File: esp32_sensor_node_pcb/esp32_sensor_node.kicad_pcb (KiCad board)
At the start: 2 copper layers, 50 x 60 mm, 27 parts, among them J1 Conn_02x10_Top_Bottom, Q1 2N7002K, SW1 SW_DIP_x01, SW2 SW_DIP_x01, U1 HT7833, U2 ESP32-WROOM-E, U3 MAX3483AEASA+

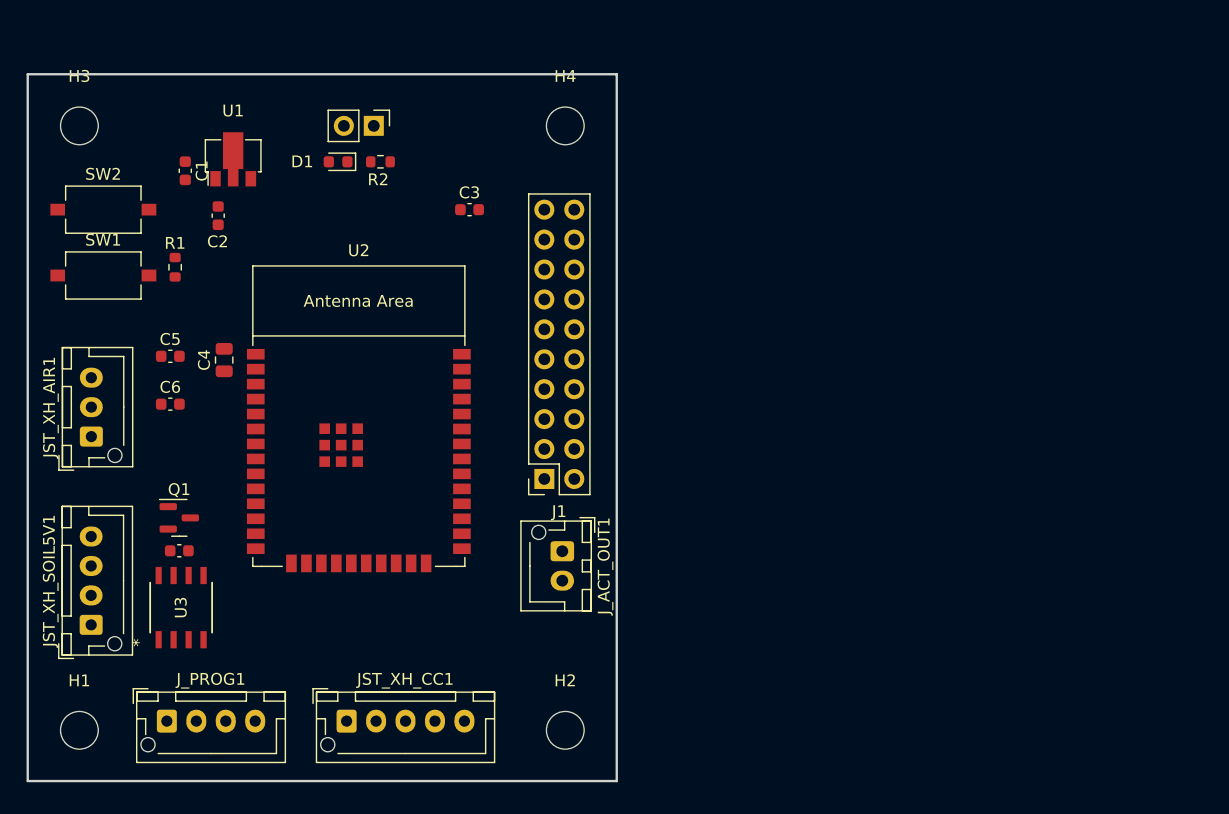
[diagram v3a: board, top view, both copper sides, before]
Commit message: Complete first draft routing
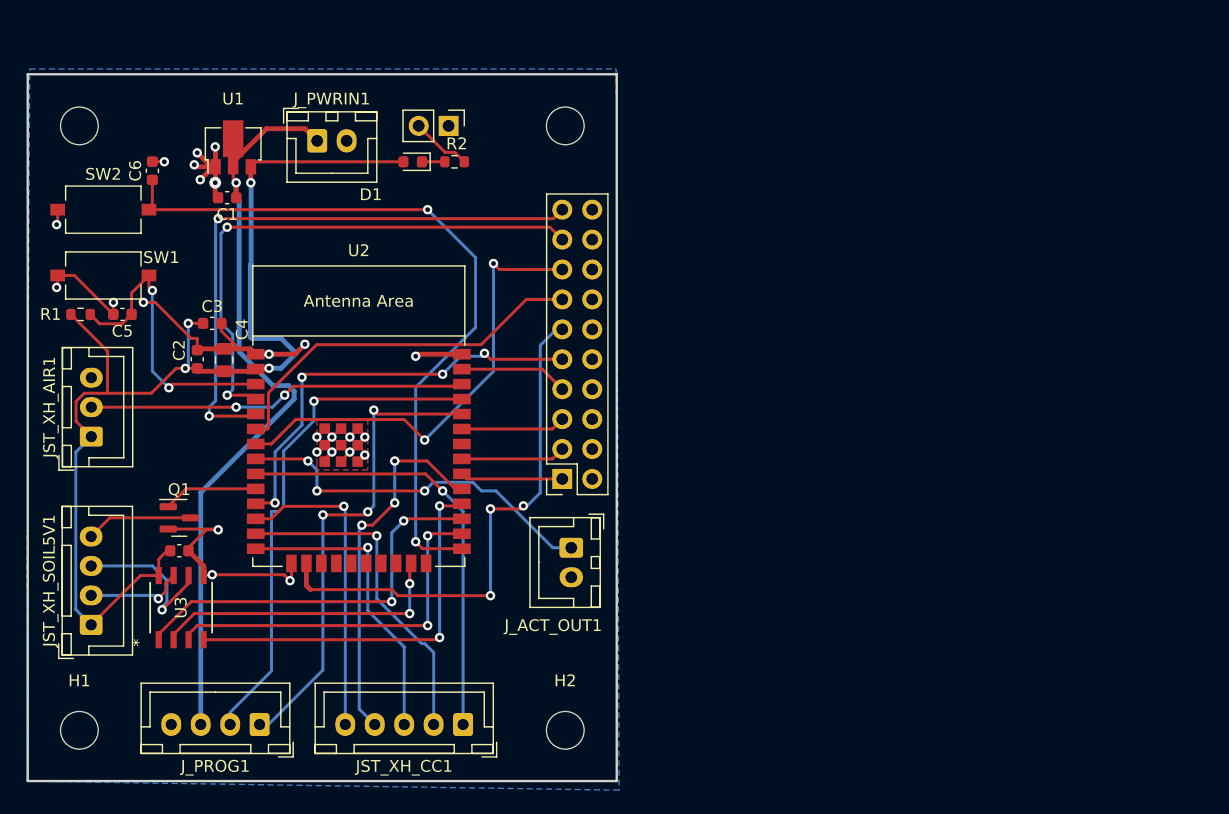
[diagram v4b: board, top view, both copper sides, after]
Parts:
- added J_PWRIN1: Conn_01x02_Socket, Connector_JST:JST_XH_B2B-XH-A_1x02_P2.50mm_Vertical, F.Cu at (44.6, 25.7)
- J1: value Conn_02x10_Top_Bottom -> Conn_02x10_Odd_Even
- JST_XH_AIR1: footprint Connector_JST:JST_XH_B3B-XH-AM_1x03_P2.50mm_Vertical -> Connector_JST:JST_XH_B3B-XH-A_1x03_P2.50mm_Vertical
- JST_XH_CC1: footprint Connector_JST:JST_XH_B5B-XH-AM_1x05_P2.50mm_Vertical -> Connector_JST:JST_XH_B5B-XH-A_1x05_P2.50mm_Vertical
- JST_XH_SOIL5V1, J_PROG1: footprint Connector_JST:JST_XH_B4B-XH-AM_1x04_P2.50mm_Vertical -> Connector_JST:JST_XH_B4B-XH-A_1x04_P2.50mm_Vertical
- J_ACT_OUT1: footprint Connector_JST:JST_XH_B2B-XH-AM_1x02_P2.50mm_Vertical -> Connector_JST:JST_XH_B2B-XH-A_1x02_P2.50mm_Vertical
- moved C3 23.9 mm to (35.7, 41.1)
- moved C6 19.9 mm to (30.6, 28.2), turned to 90 degrees
- moved C2 12.3 mm to (34.4, 44.2), turned to 90 degrees
- moved JST_XH_CC1 9.89 mm to (57.0, 75.2), turned to 180 degrees
- moved R1 8.97 mm to (24.5, 40.4), turned to 0 degrees
- moved J_PROG1 7.88 mm to (39.7, 75.2), turned to 180 degrees
- moved JP1 6.35 mm to (55.7, 24.4)
- moved D1 6.33 mm to (52.7, 27.4)
- moved R2 6.29 mm to (56.2, 27.4), turned to 180 degrees
- moved C5 5.40 mm to (28.0, 40.4), turned to 180 degrees
- moved C1 4.23 mm to (36.9, 30.5), turned to 180 degrees
- moved J1 1.52 mm to (65.4, 54.4)
- moved U1 1.02 mm to (37.4, 25.9)
- moved J_ACT_OUT1 0.82 mm to (66.1, 60.2)
- turned C7_MAXDECOUP1 to 0 degrees
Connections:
- J1 pad 10: GPIO39 -> GND
- J1 pad 11: GND -> GPIO13
- J1 pad 13: GND -> GPIO34
- J1 pad 15: GND -> GPIO35
- J1 pad 17: GND -> GPIO36
- J1 pad 19: GND -> GPIO39
- J1 pad 2: GPIO19 -> GND
- J1 pad 3: GPIO21 -> GPIO19
- J1 pad 4: GPIO23 -> GND
- J1 pad 5: GPIO26 -> GPIO21
- J1 pad 6: GPIO13 -> GND
- J1 pad 7: GPIO34 -> GPIO23
- J1 pad 8: GPIO35 -> GND
- J1 pad 9: GPIO36 -> GPIO26
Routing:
- net +3.3V: track 0.00 -> 96.2 mm, vias 0 -> 4
- net GND: track 0.00 -> 69.6 mm, vias 0 -> 24
- net +5V: track 0.00 -> 64.7 mm, vias 0 -> 1
- net GPIO0/BOOT: track 0.00 -> 62.0 mm, vias 0 -> 2
- net GPIO39: track 0.00 -> 50.4 mm, vias 0 -> 2
- net GPIO36: track 0.00 -> 46.5 mm, vias 0 -> 2
- net GPIO13: track 0.00 -> 44.5 mm, vias 0 -> 3
- net Net-(J_PROG1-Pin_2): track 0.00 -> 44.1 mm, vias 0 -> 1
- net Net-(J_PROG1-Pin_1): track 0.00 -> 41.1 mm, vias 0 -> 3
- net GPIO35: track 0.00 -> 39.4 mm, vias 0 -> 2
- net ACT_IN: track 0.00 -> 37.0 mm, vias 0 -> 1
- net GPIO26: track 0.00 -> 36.3 mm, vias 0 -> 4
- net Net-(U2-GPIO16): track 0.00 -> 33.2 mm, vias 0 -> 2
- net Net-(U2-GPIO17): track 0.00 -> 33.0 mm, vias 0 -> 2
- net GPIO34: track 0.00 -> 32.3 mm
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- added copper zone on B.Cu, net GND
- added copper zone on F.Cu, net GND

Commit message: Changed schematic - 3.3V to RS485, 5V to Soil sensor. Changed resistor from 1.9k to 4.7k. Finished routing of PCB with new schematic
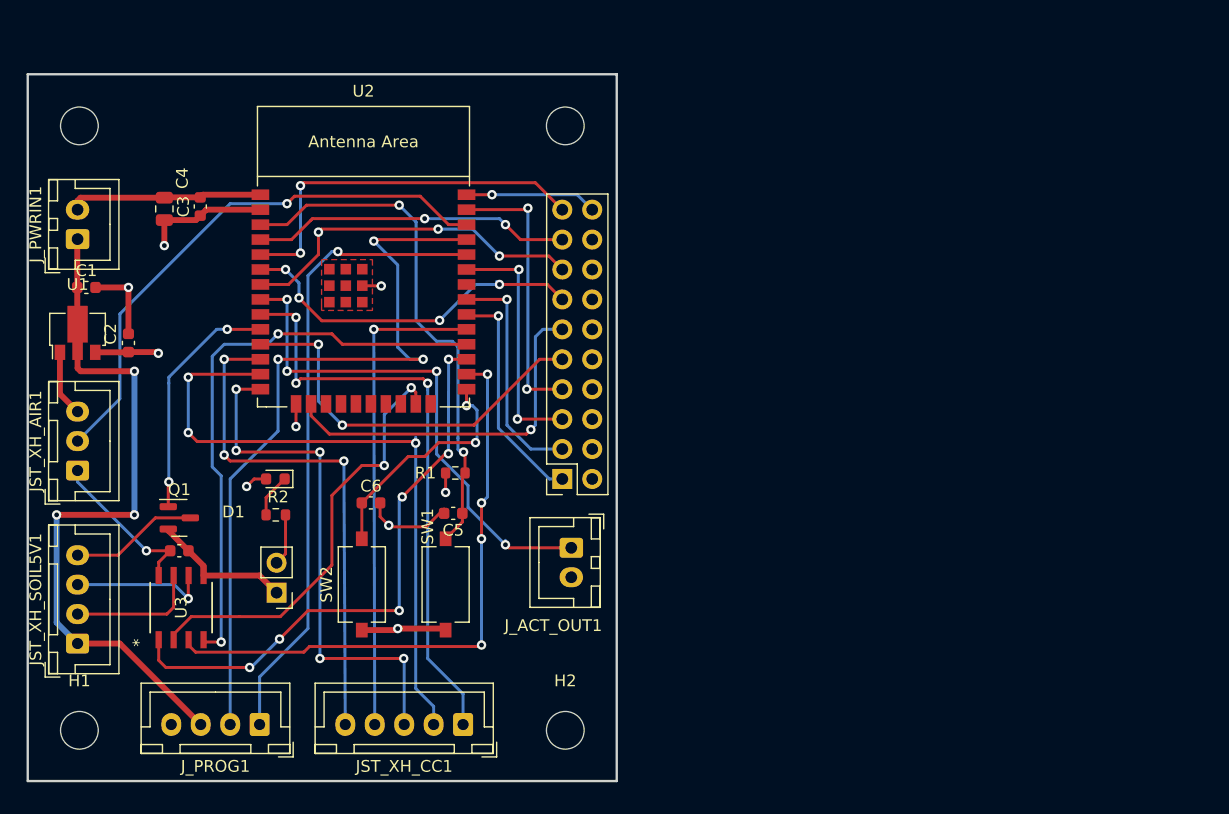
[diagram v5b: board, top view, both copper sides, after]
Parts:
- R2: value 1.91K -> 4.7K
- moved JP1 42.2 mm to (41.1, 64.0), turned to 180 degrees
- moved SW1 39.1 mm to (55.5, 63.3), turned to 90 degrees
- moved SW2 38.6 mm to (48.4, 63.3), turned to 90 degrees
- moved R1 34.5 mm to (56.3, 53.8)
- moved C6 33.8 mm to (49.1, 56.4), turned to 0 degrees
- moved R2 33.6 mm to (41.1, 57.4)
- moved C5 32.8 mm to (56.1, 57.3)
- moved D1 29.3 mm to (41.0, 54.4)
- moved J_PWRIN1 22.0 mm to (24.2, 34.0), turned to 90 degrees
- moved U1 20.6 mm to (24.2, 41.7)
- moved C1 14.2 mm to (25.0, 38.1), turned to 0 degrees
- moved C4 13.8 mm to (31.6, 31.4)
- moved U2 13.5 mm to (48.5, 37.2)
- moved C3 9.97 mm to (34.6, 31.2), turned to 90 degrees
- moved C2 6.00 mm to (28.5, 42.8)
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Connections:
- JST_XH_SOIL5V1 pad 1: +3.3V -> +5V
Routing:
- net +3.3V: track 96.2 -> 33.4 mm, vias 4 -> 5
- net GPIO0/BOOT: track 62.0 -> 20.1 mm
- net TX_CC: track 28.5 -> 55.6 mm, vias 1 -> 3
- net Net-(J_PROG1-Pin_2): track 44.1 -> 65.4 mm, vias 1 -> 3
- net Net-(U2-ADC2_CH0/GPIO4): track 31.2 -> 50.9 mm, vias 2 -> 4
- net GPIO36: track 46.5 -> 27.1 mm
- net RESET: track 25.8 -> 44.9 mm
- net RX_CC: track 25.9 -> 44.7 mm, vias 1 -> 5
- net GPIO39: track 50.4 -> 32.4 mm
- net WKP: track 26.5 -> 44.1 mm, vias 1 -> 3
- net Net-(U2-GPIO16): track 33.2 -> 49.2 mm, vias 2 -> 6
- net Net-(U2-GPIO17): track 33.0 -> 48.9 mm
- net Net-(JST_XH_AIR1-Pin_2): track 32.0 -> 47.4 mm, vias 2 -> 1
- net GPIO23: track 9.23 -> 23.7 mm, vias 0 -> 2
- net ACT_IN: track 37.0 -> 50.4 mm, vias 1 -> 3
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- added copper zone on In2.Cu, net +3.3V
- added copper zone on In1.Cu, net GND
- removed copper zone on B.Cu, net GND
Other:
- copper layers 2 -> 4

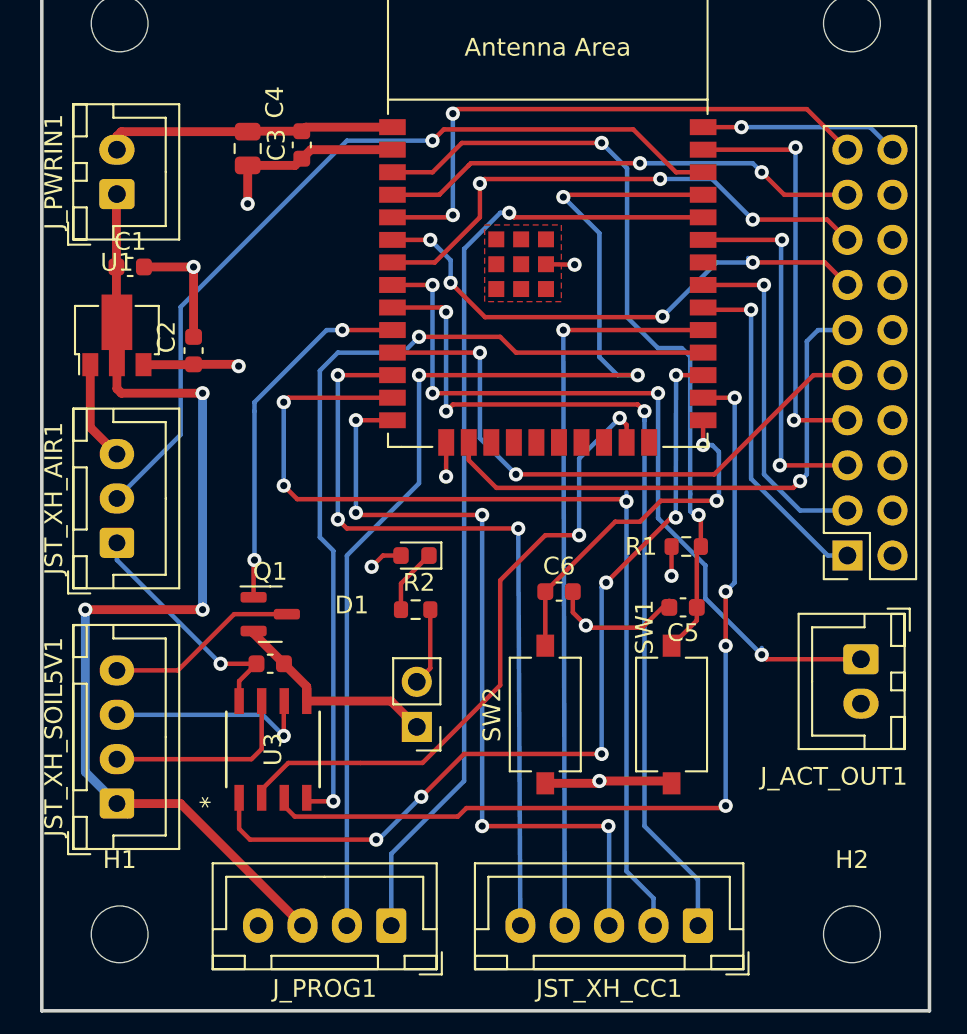
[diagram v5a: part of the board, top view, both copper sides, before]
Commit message: Add transfer vias for all HSS, remove some routing voids, standardize track lengths for power and signal
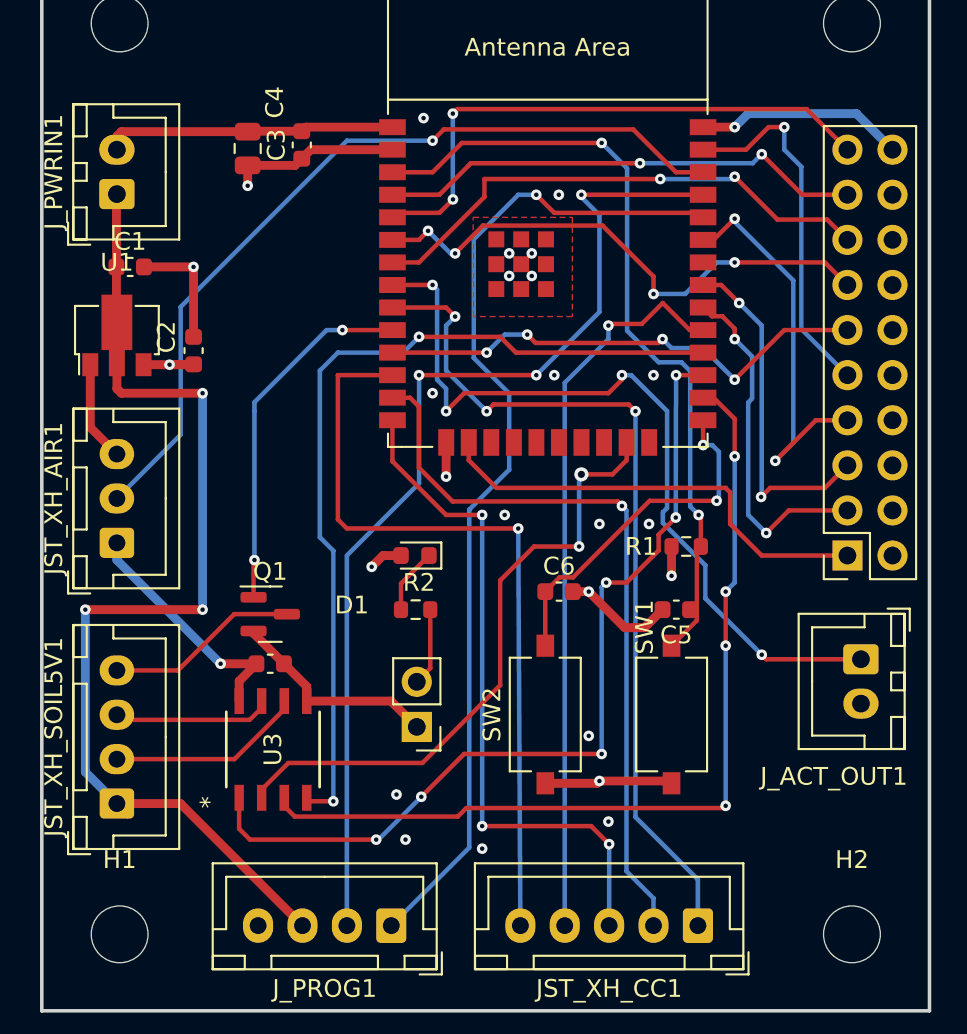
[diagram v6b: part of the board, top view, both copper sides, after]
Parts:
- moved C5 0.40 mm to (55.7, 57.4)
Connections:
- J1 pad 1: GPIO18 -> GPIO13
- J1 pad 11: GPIO13 -> GPIO26
- J1 pad 3: GPIO19 -> GPIO18
- J1 pad 5: GPIO21 -> GPIO19
- J1 pad 7: GPIO23 -> GPIO21
- J1 pad 9: GPIO26 -> GPIO23
- U3 pad 6: Net-(JST_XH_SOIL5V1-Pin_3) -> Net-(JST_XH_SOIL5V1-Pin_2)
- U3 pad 7: Net-(JST_XH_SOIL5V1-Pin_2) -> Net-(JST_XH_SOIL5V1-Pin_3)
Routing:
- net TX_CC: track 55.6 -> 41.8 mm, vias 3 -> 1
- net Net-(J_PROG1-Pin_2): track 65.4 -> 58.1 mm
- net RX_CC: track 44.7 -> 38.3 mm, vias 5 -> 3
- net GPIO13: track 31.0 -> 25.6 mm, vias 1 -> 0
- net GPIO26: track 33.6 -> 28.4 mm, vias 2 -> 4
- net GPIO23: track 23.7 -> 20.5 mm, vias 2 -> 1
- net Net-(JST_XH_SOIL5V1-Pin_3): track 11.9 -> 8.93 mm, vias 1 -> 0
- net Net-(J_PROG1-Pin_1): track 54.2 -> 56.7 mm
- net +3.3V: track 33.4 -> 31.1 mm
- net GND: track 70.5 -> 68.3 mm, vias 6 -> 22
- net GPIO21: track 21.0 -> 22.7 mm
- net Net-(J_ACT_OUT1-Pin_1): track 44.3 -> 45.8 mm
- net RS485_*RE: track 36.8 -> 35.5 mm
- net ACT_IN: track 50.4 -> 49.4 mm
- net Net-(U2-ADC2_CH0/GPIO4): track 50.9 -> 50.2 mm
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
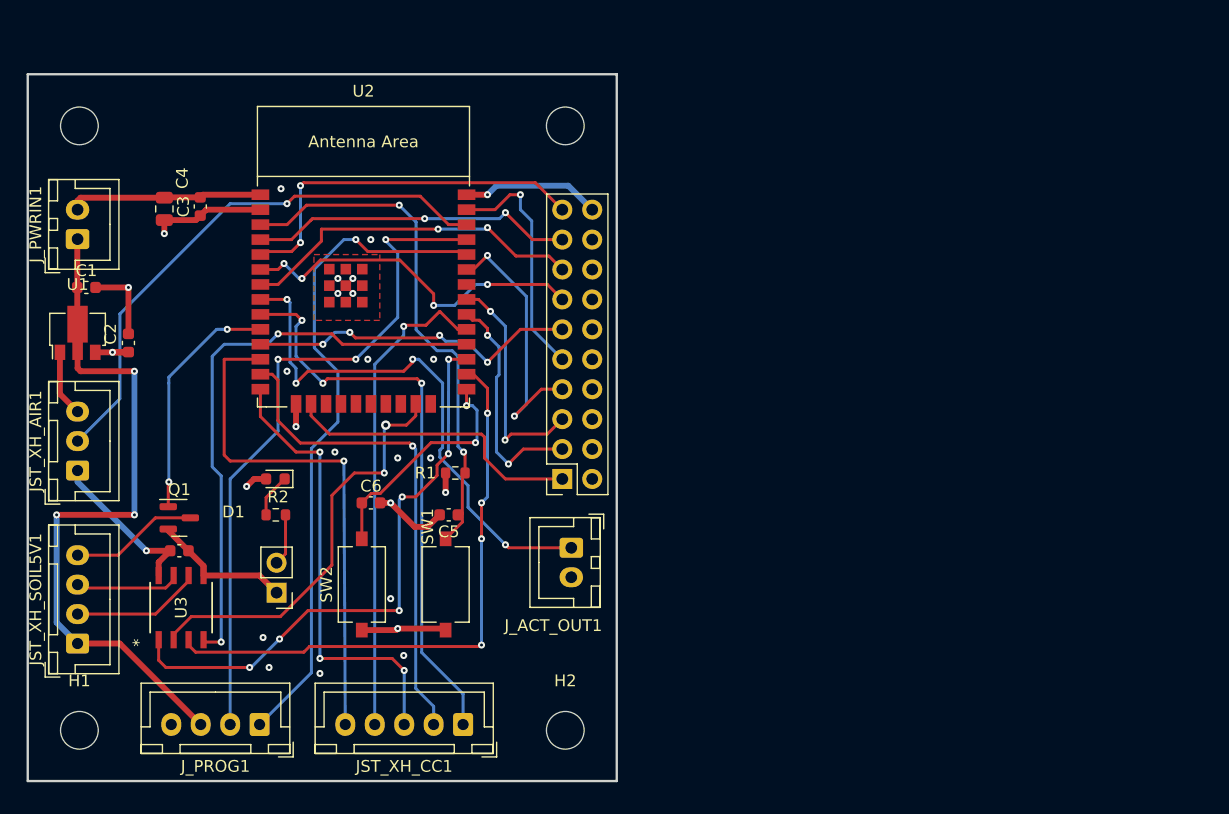
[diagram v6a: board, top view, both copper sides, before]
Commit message: Center MCU, reroute cleanup, add labels and shift components to fit
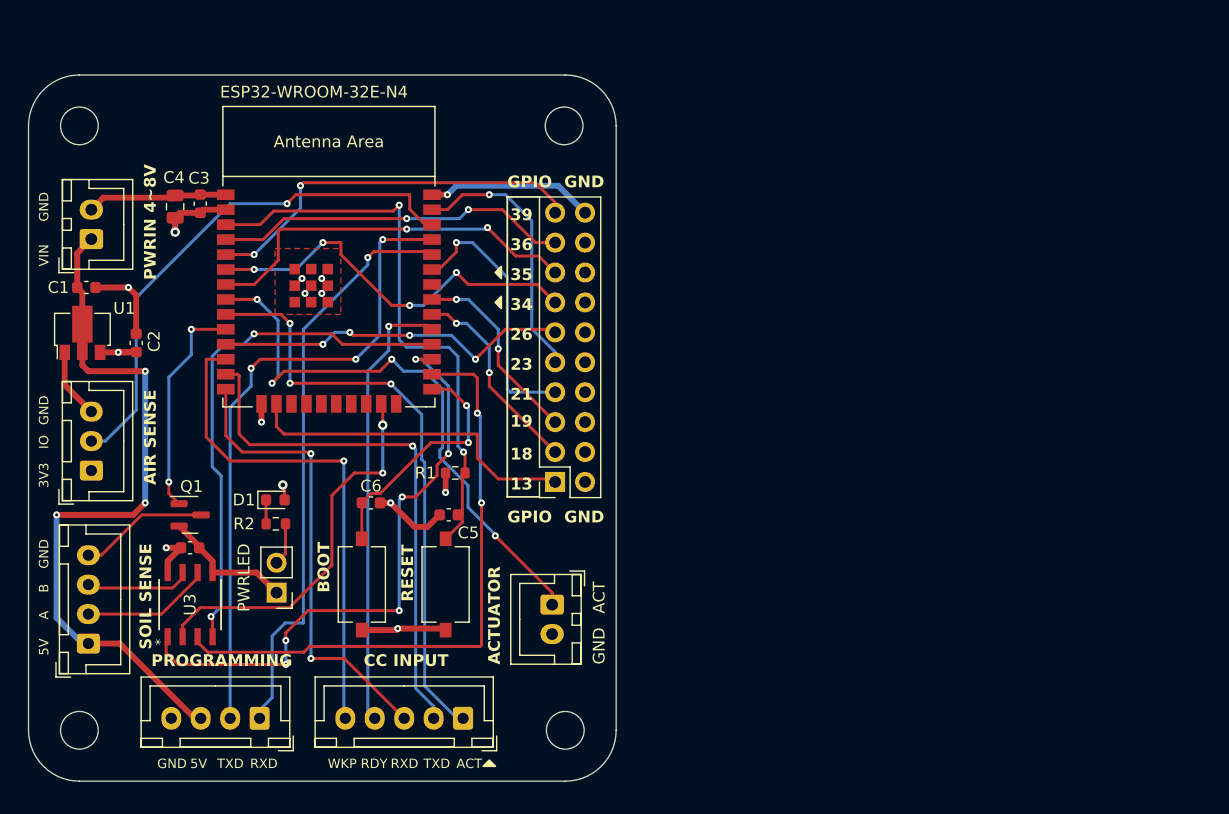
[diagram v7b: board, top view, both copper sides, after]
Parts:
- moved J_ACT_OUT1 5.09 mm to (64.5, 65.0)
- moved U2 2.93 mm to (45.6, 37.2)
- moved D1 1.78 mm to (41.0, 56.1), turned to 0 degrees
- moved JST_XH_AIR1 1.17 mm to (25.4, 53.6)
- moved J_PWRIN1 1.17 mm to (25.4, 34.0)
- moved C7_MAXDECOUP1 0.95 mm to (33.8, 60.2)
- moved Q1 0.95 mm to (33.8, 57.4)
- moved C4 0.94 mm to (32.5, 31.2)
- moved JST_XH_SOIL5V1 0.92 mm to (25.1, 68.3)
- moved U3 0.80 mm to (33.8, 65.0)
- moved R2 0.76 mm to (41.1, 58.2)
- moved C2 0.66 mm to (29.2, 42.8)
- moved J1 0.66 mm to (64.8, 54.6)
- moved JST_XH_CC1 0.52 mm to (57.0, 74.7)
- moved J_PROG1 0.52 mm to (39.7, 74.7)
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- renumbered SW2 to BOOT
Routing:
- net +3.3V: track 31.1 -> 16.5 mm
- net Net-(J_PROG1-Pin_1): track 56.7 -> 48.5 mm
- net Net-(U2-GPIO17): track 48.9 -> 44.3 mm
- net RESET: track 44.7 -> 48.5 mm
- net Net-(J_ACT_OUT1-Pin_1): track 45.8 -> 49.4 mm
- net GND: track 68.3 -> 65.0 mm, vias 22 -> 9
- net GPIO34: track 30.6 -> 33.9 mm
- net GPIO35: track 29.7 -> 33.0 mm
- net TX_CC: track 41.8 -> 45.1 mm
- net RDY: track 41.3 -> 38.1 mm
- net Net-(J_PROG1-Pin_2): track 58.1 -> 54.9 mm
- net Net-(JST_XH_AIR1-Pin_2): track 47.4 -> 44.4 mm
- net RS485_*RE: track 35.5 -> 32.5 mm
- net GPIO19: track 19.5 -> 16.6 mm
- net GPIO18: track 19.8 -> 16.9 mm
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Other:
- board size 50 x 60 mm -> 49.9 x 59.9 mm
- board text added: "13"
- board text added: "18"
- board text added: "19"
- board text added: "21"
- board text added: "23"
- board text added: "26"
- board text added: "34"
- board text added: "35"
- board text added: "36"
- board text added: "39"
- board text added: "3V3"
- board text added: "5V"
- board text added: "A"
- board text added: "ACT"
- board text added: "ACTUATOR"
- board text added: "AIR SENSE"
- board text added: "B"
- board text added: "BOOT"
- board text added: "CC INPUT"
- board text added: "ESP32-WROOM-32E-N4"
- board text added: "GND"
- board text added: "GPIO"
- board text added: "IO"
- board text added: "PROGRAMMING"
- board text added: "PWRIN 4~8V"
- board text added: "PWRLED"
- board text added: "RDY"
- board text added: "RESET"
- board text added: "RXD"
- board text added: "SOIL SENSE"
- board text added: "TXD"
- board text added: "VIN"
- board text added: "WKP"
